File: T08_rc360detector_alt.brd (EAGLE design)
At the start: 100 x 80 mm, 55 parts, among them IC1 LM317MSTT3, IC2 LM317MSTT3, IC3 LM1117, U2 ATMEGA328P_PDIP, X1 SSW-101-02-S-D, X3 SSW-101-02-S-D, X4 87758-0616, X5 87758-0616, X6 SSW-104-02-S-Q

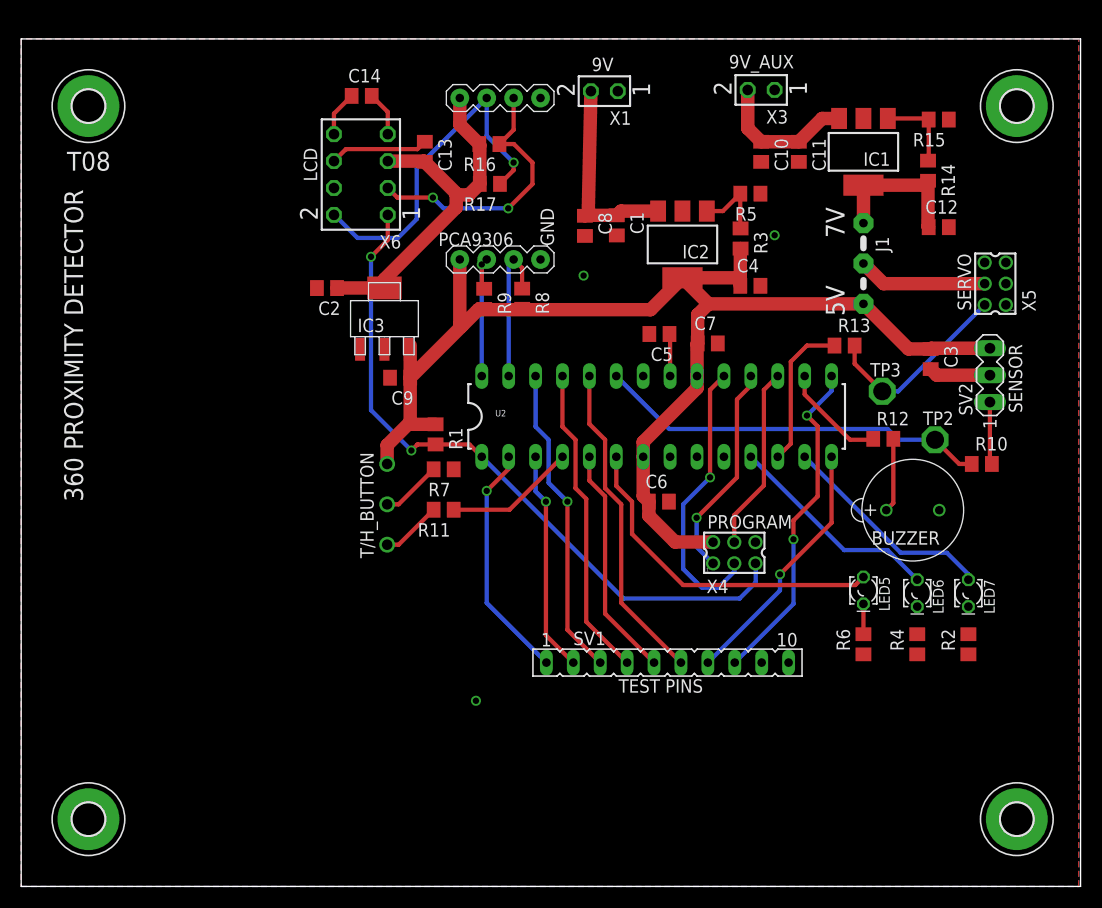
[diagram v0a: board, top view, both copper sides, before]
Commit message: Finished preliminary layout
Finished layout after feedback today
Also made an alternate layout that I feel is cleaner and experimented
with importing silkscreen images.
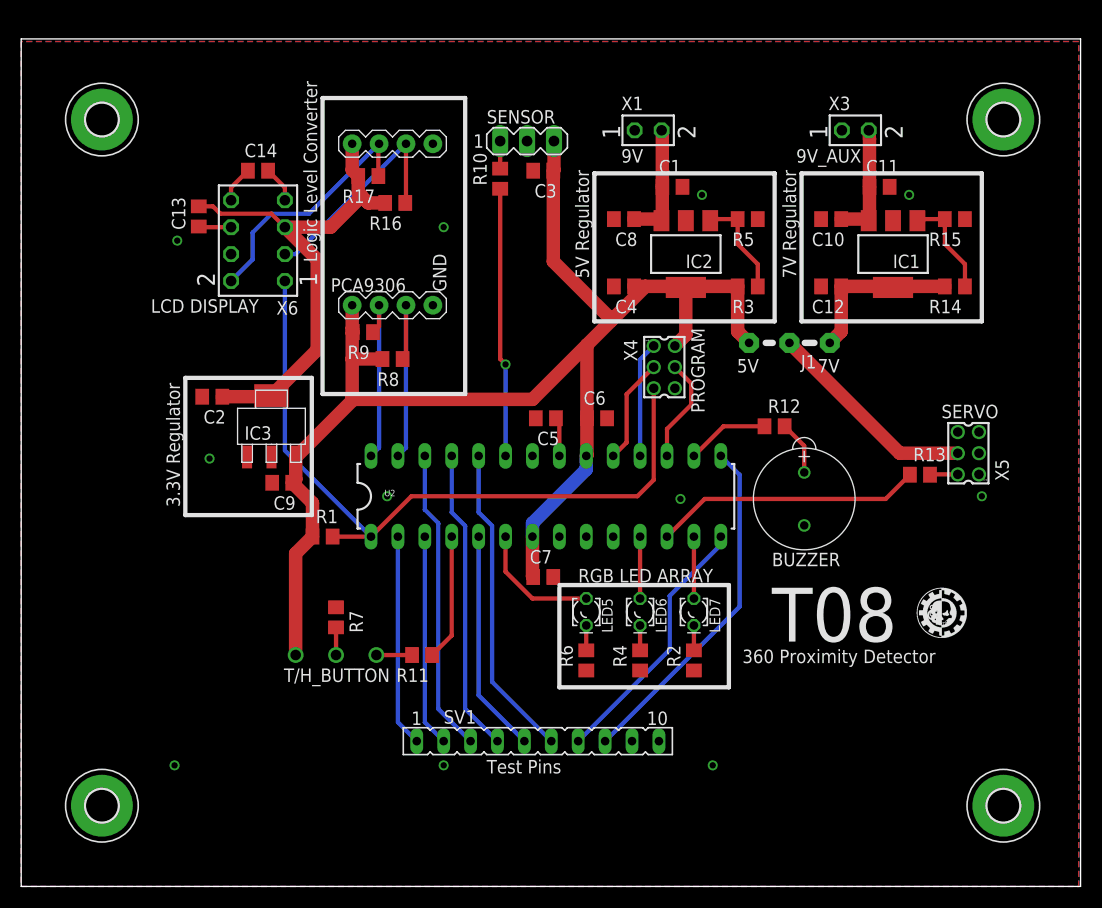
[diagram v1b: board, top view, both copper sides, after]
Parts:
- removed SV2: (no value), con-lstb:MA03-1
- removed TP2, TP3: TPPAD1-17, testpad:P1-17
- added SENSOR: (no value), con-lstb:MA03-1
- moved H1 108.7 mm to (92.7, 72.4)
- moved H3 86.4 mm to (7.62, 72.4)
- moved H4 66.1 mm to (7.62, 7.62)
- moved R10 52.8 mm to (45.2, 66.8), turned to 90 degrees
- moved C3 40.7 mm to (49.3, 67.6), turned to 180 degrees
- moved C7 27.0 mm to (49.3, 29.2)
- moved LED5 26.2 mm to (53.3, 25.9)
- moved LED6 26.2 mm to (58.4, 25.9)
- moved R4 26.2 mm to (58.4, 21.3)
- moved R6 26.2 mm to (53.3, 21.3)
- moved LED7 26.0 mm to (63.5, 25.9)
- moved R2 26.0 mm to (63.5, 21.3)
- moved C13 22.2 mm to (16.8, 63.2), turned to 90 degrees
- moved X4 18.7 mm to (60.7, 49.0), turned to 270 degrees
- moved R7 17.3 mm to (29.7, 25.4), turned to 270 degrees
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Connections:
- removed net TP8: SV1.9
- removed net TP9: SV1.10
- net +5V: now also SENSOR.3; no longer SV2.3
- net GND: now also SENSOR.2; no longer SV2.2
- net PROX_ANALOG: now also SENSOR.1; no longer SV2.1
- net PROX_ANALOG_R: no longer TP2.TP
- net SERVO_PWM: no longer TP3.TP
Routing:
- net LED0: track 32.1 -> 12.0 mm
- net PROG_SCK: track 26.8 -> 9.97 mm, vias 1 -> 0
- net SERVO_PWM: track 18.4 -> 2.64 mm
- net +5V: track 122.0 -> 136.9 mm
- net LED2: track 20.6 -> 5.84 mm
- net LED1: track 20.5 -> 5.84 mm
- net +3V3: track 35.5 -> 48.8 mm
- net PROX_ANALOG_R: track 37.0 -> 25.4 mm, vias 0 -> 1
- net SERVO_PWM_R: track 14.6 -> 25.3 mm
- net PROG_MISO: track 20.4 -> 10.9 mm, vias 1 -> 0
- net SCL_BUF: track 33.3 -> 23.9 mm, vias 1 -> 0
- net N$16: track 12.2 -> 20.2 mm
- net VBP: track 19.0 -> 11.2 mm
- net PROG_MOSI: track 17.4 -> 9.97 mm
- net N$18: track 9.33 -> 3.08 mm
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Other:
- board text added: "3.3V Regulator"
- board text added: "360 Proximity Detector"
- board text added: "5V Regulator"
- board text added: "7V Regulator"
- board text added: "LCD DISPLAY"
- board text added: "Logic Level Converter"
- board text added: "RGB LED ARRAY"
- board text added: "Test Pins"
- board text removed: "360 PROXIMITY DETECTOR"
- board text removed: "LCD"
- board text removed: "SENSOR"
- board text removed: "TEST PINS"

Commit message: Slight changes. Passed DRC
Made sure DRC worked and had updated libraries. This should work now,
(hopefully)
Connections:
- net GND: now also CX-0905C.OUT; no longer CX-0905C.P$2
- net N$4: now also CX-0905C.IN; no longer CX-0905C.P$1
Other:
- board text added: "+"
- board text added: "1"
